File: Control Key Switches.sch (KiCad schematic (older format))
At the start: 64 parts

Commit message: Corrected errors found in design rule check
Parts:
- removed C? (x16): .047u, symbol Device:C
- removed R? (x32): 10k, symbol Device:R
- removed SW?: PRINT SCREEN, symbol Switch:SW_Push
- removed SW?: INSERT, symbol Switch:SW_Push
- removed SW?: DELETE, symbol Switch:SW_Push
- removed SW?: EXT8, symbol Switch:SW_Push
- removed SW?: LEFT, symbol Switch:SW_Push
- removed SW?: SCRL, symbol Switch:SW_Push
- removed SW?: HOME, symbol Switch:SW_Push
- removed SW?: END, symbol Switch:SW_Push
- removed SW?: EXT9, symbol Switch:SW_Push
- removed SW?: UP, symbol Switch:SW_Push
- removed SW?: DOWN, symbol Switch:SW_Push
- removed SW?: PAUSE, symbol Switch:SW_Push
- removed SW?: PAGE UP, symbol Switch:SW_Push
- removed SW?: PAGE DOWN, symbol Switch:SW_Push
- removed SW?: EXT10, symbol Switch:SW_Push
- removed SW?: RIGHT, symbol Switch:SW_Push
- added C45, C46, C47, C48, C49, C50, C51, C52, C53, C54, C55, C56, C57, C58, C59, C60: .047u, Capacitor_SMD:C_1206_3216Metric_Pad1.42x1.75mm_HandSolder, symbol Device:C
- added R100, R101, R102, R103, R104, R105, R106, R107, R108, R109, R110, R111, R112, R113, R114, R115, R116, R117, R118, R119, R120, R121, R122, R123, R124, R125, R126, R127, R128, R97, R98, R99: 10k, Resistor_SMD:R_1206_3216Metric_Pad1.42x1.75mm_HandSolder, symbol Device:R
- added SW32: PRINT SCREEN, Button_Switch_Keyboard:SW_Cherry_MX_1.00u_PCB, symbol Switch:SW_Push
- added SW33: SCRL, Button_Switch_Keyboard:SW_Cherry_MX_1.00u_PCB, symbol Switch:SW_Push
- added SW34: PAUSE, Button_Switch_Keyboard:SW_Cherry_MX_1.00u_PCB, symbol Switch:SW_Push
- added SW35: INSERT, Button_Switch_Keyboard:SW_Cherry_MX_1.00u_PCB, symbol Switch:SW_Push
- added SW36: HOME, Button_Switch_Keyboard:SW_Cherry_MX_1.00u_PCB, symbol Switch:SW_Push
- added SW37: PAGE UP, Button_Switch_Keyboard:SW_Cherry_MX_1.00u_PCB, symbol Switch:SW_Push
- added SW38: DELETE, Button_Switch_Keyboard:SW_Cherry_MX_1.00u_PCB, symbol Switch:SW_Push
- added SW39: END, Button_Switch_Keyboard:SW_Cherry_MX_1.00u_PCB, symbol Switch:SW_Push
- added SW40: PAGE DOWN, Button_Switch_Keyboard:SW_Cherry_MX_1.00u_PCB, symbol Switch:SW_Push
- added SW41: EXT8, Button_Switch_Keyboard:SW_Cherry_MX_1.00u_PCB, symbol Switch:SW_Push
- added SW42: EXT9, Button_Switch_Keyboard:SW_Cherry_MX_1.00u_PCB, symbol Switch:SW_Push
- added SW43: EXT10, Button_Switch_Keyboard:SW_Cherry_MX_1.00u_PCB, symbol Switch:SW_Push
- added SW44: UP, Button_Switch_Keyboard:SW_Cherry_MX_1.00u_PCB, symbol Switch:SW_Push
- added SW45: LEFT, Button_Switch_Keyboard:SW_Cherry_MX_1.00u_PCB, symbol Switch:SW_Push
- added SW46: DOWN, Button_Switch_Keyboard:SW_Cherry_MX_1.00u_PCB, symbol Switch:SW_Push
- added SW47: RIGHT, Button_Switch_Keyboard:SW_Cherry_MX_1.00u_PCB, symbol Switch:SW_Push
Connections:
- net 3.3V: now also R103.1, R104.1, R105.1, R109.1, R110.1, R111.1, R115.1, R116.1, R117.1, R121.1, R123.1, R124.1, R125.1, R97.1, R98.1, R99.1
- net DEL: now also C51.2, R112.2
- net DN: now also C59.2, R127.2
- net END: now also C52.2, R113.2
- net EXT10: now also C56.2, R120.2
- net EXT8: now also C54.2, R118.2
- net EXT9: now also C55.2, R119.2
- net GND: now also C45.1, C46.1, C47.1, C48.1, C49.1, C50.1, C51.1, C52.1, C53.1, C54.1, C55.1, C56.1, C57.1, C58.1, C59.1, C60.1, SW32.2, SW33.2, SW34.2, SW35.2, SW36.2, SW37.2, SW38.2, SW39.2, SW40.2, SW41.2, SW42.2, SW43.2, SW44.2, SW45.2, SW46.2, SW47.2
- net HOME: now also C49.2, R107.2
- net INS: now also C48.2, R106.2
- net LT: now also C58.2, R126.2
- net PAUS: now also C47.2, R102.2
- net PGDN: now also C53.2, R114.2
- net PGUP: now also C50.2, R108.2
- net PRNT: now also C45.2, R100.2
- net RT: now also C60.2, R128.2
- net SCRL: now also C46.2, R101.2
- net UP: now also C57.2, R122.2
- new net: R101.1, R98.2, SW33.1
- new net: R103.2, R106.1, SW35.1
- new net: R104.2, R107.1, SW36.1
- new net: R105.2, R108.1, SW37.1
- new net: R110.2, R113.1, SW39.1
- new net: R121.2, R122.1, SW44.1
- new net: R117.2, R120.1, SW43.1
- new net: R116.2, R119.1, SW42.1
- new net: R111.2, R114.1, SW40.1
- new net: R100.1, R97.2, SW32.1
- new net: R102.1, R99.2, SW34.1
- new net: R124.2, R127.1, SW46.1
- new net: R115.2, R118.1, SW41.1
- new net: R109.2, R112.1, SW38.1
- new net: R125.2, R128.1, SW47.1
- new net: R123.2, R126.1, SW45.1

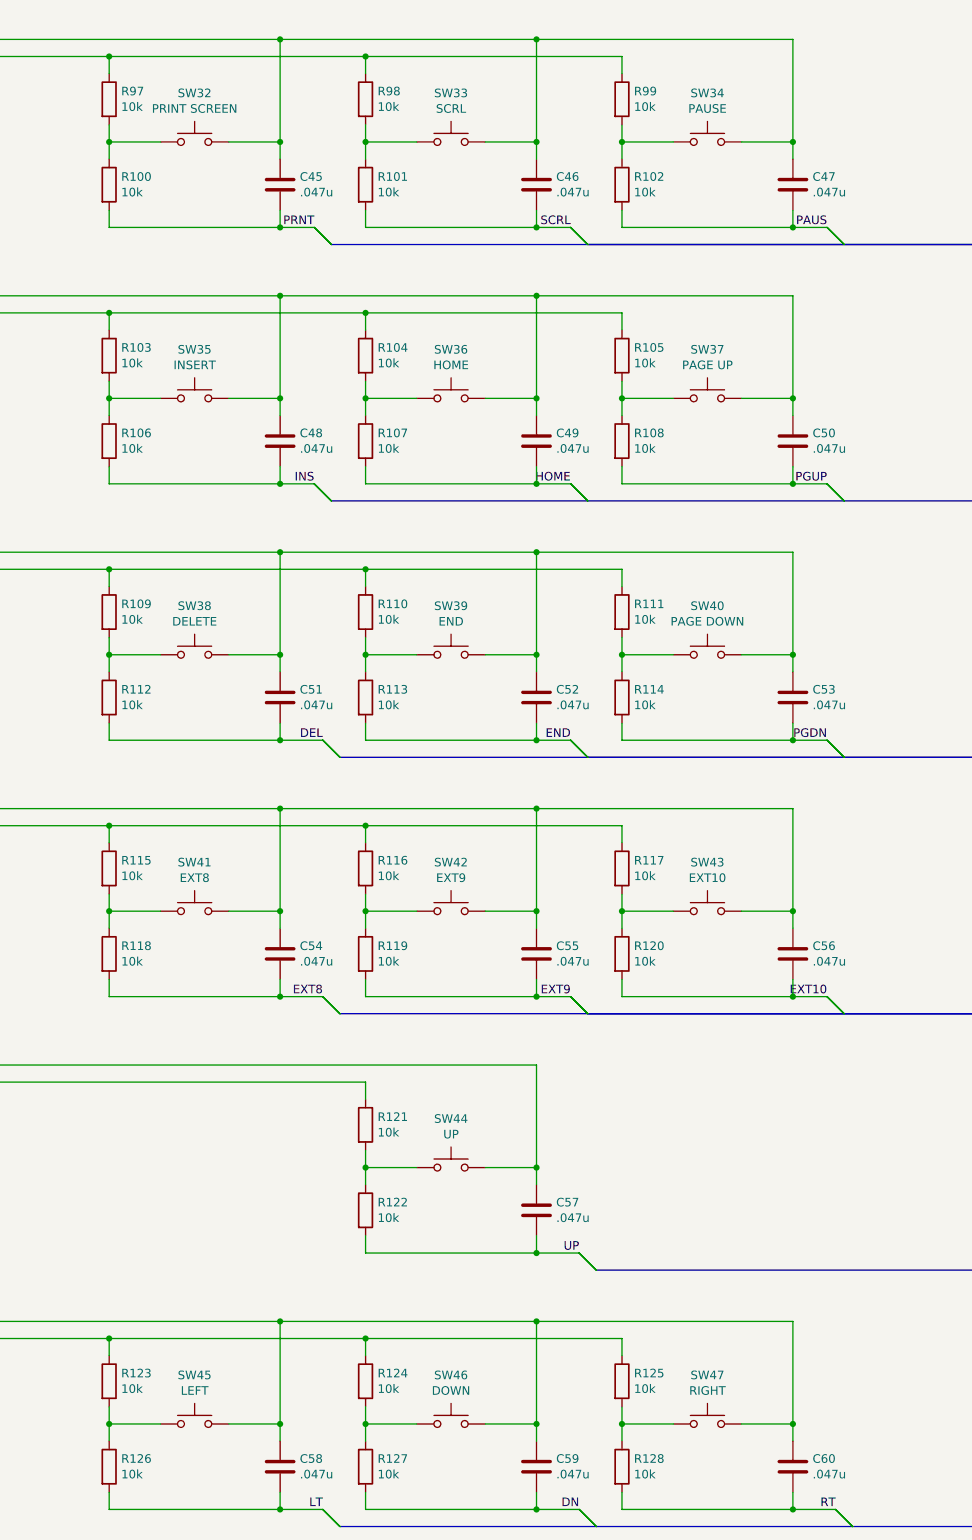
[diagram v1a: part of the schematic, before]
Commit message: Redesigned for single large PCB
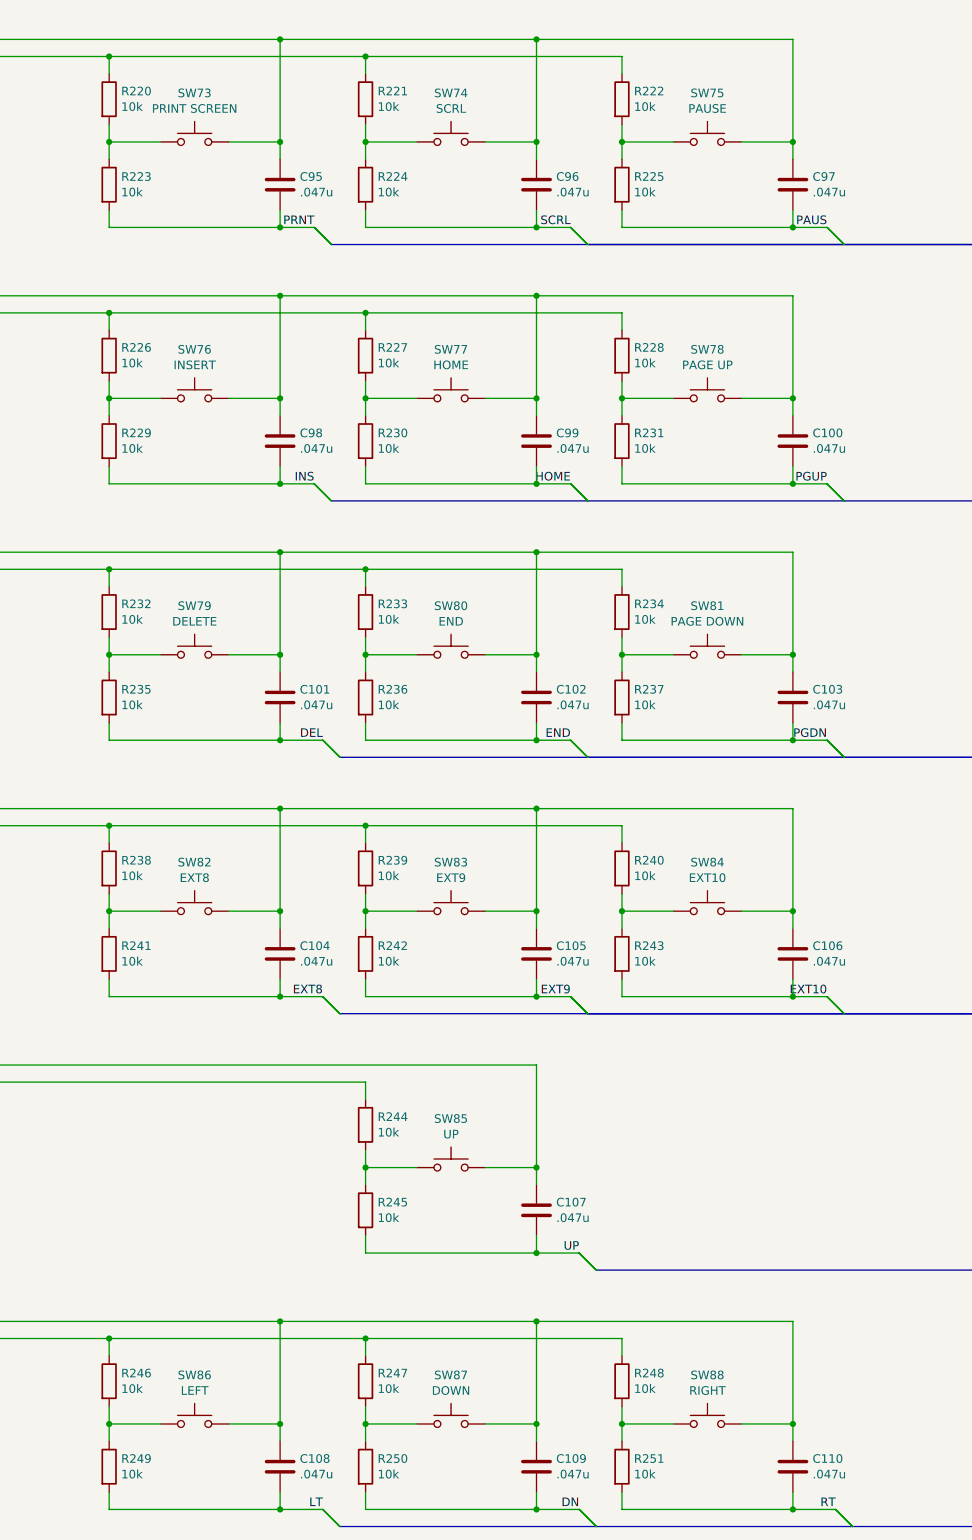
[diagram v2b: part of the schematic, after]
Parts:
- renumbered C50 to C100, C51 to C101, C52 to C102, C53 to C103, C54 to C104, C55 to C105, C56 to C106, C57 to C107, C58 to C108, C59 to C109, C60 to C110, C45 to C95, C46 to C96, C47 to C97, C48 to C98, C49 to C99, R97 to R220, R98 to R221, R99 to R222, R100 to R223, R101 to R224, R102 to R225, R103 to R226, R104 to R227, R105 to R228, R106 to R229, R107 to R230, R108 to R231, R109 to R232, R110 to R233, R111 to R234, R112 to R235, R113 to R236, R114 to R237, R115 to R238, R116 to R239, R117 to R240, R118 to R241, R119 to R242, R120 to R243, R121 to R244, R122 to R245, R123 to R246, R124 to R247, R125 to R248, R126 to R249, R127 to R250, R128 to R251, SW32 to SW73, SW33 to SW74, SW34 to SW75, SW35 to SW76, SW36 to SW77, SW37 to SW78, SW38 to SW79, SW39 to SW80, SW40 to SW81, SW41 to SW82, SW42 to SW83, SW43 to SW84, SW44 to SW85, SW45 to SW86, SW46 to SW87, SW47 to SW88
